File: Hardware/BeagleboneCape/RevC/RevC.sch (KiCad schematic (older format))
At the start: 6 parts, among them P1 CONN_02X04, P2 CONN_01X12, P8 BeagleBone_Black_Header, P9 BeagleBone_Black_Header

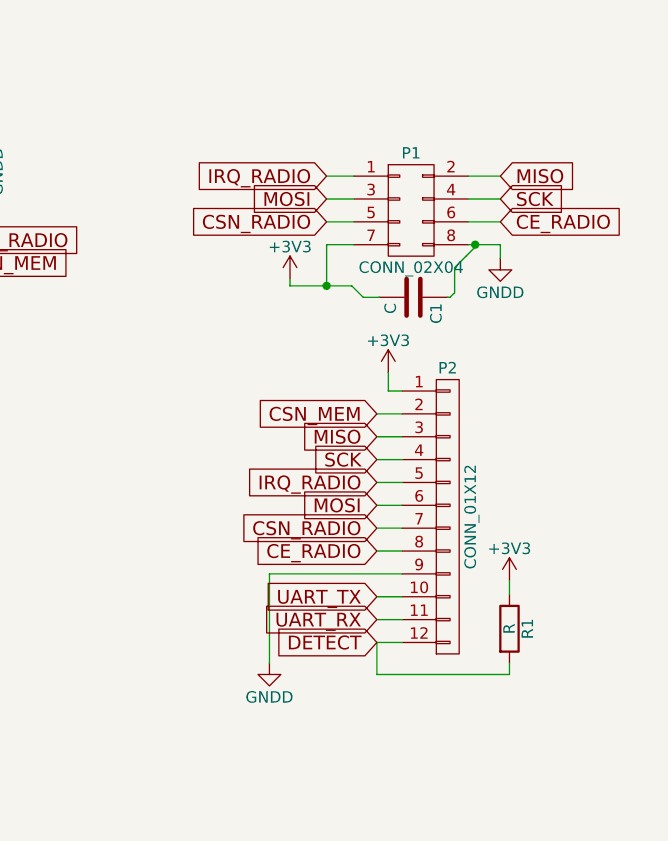
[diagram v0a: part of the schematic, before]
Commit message: initial mockup of board layout, removed 8 pin connector in favour of the single-module board
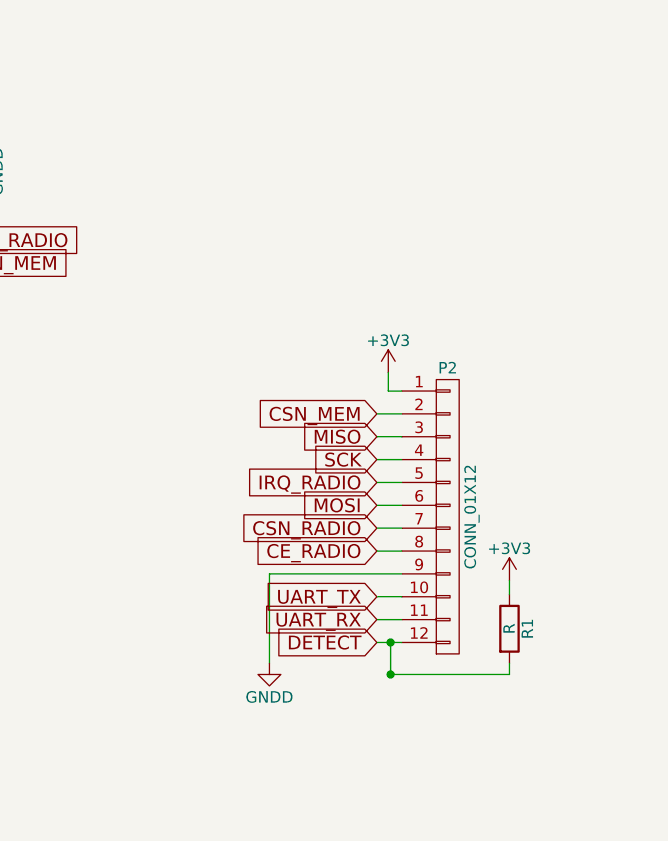
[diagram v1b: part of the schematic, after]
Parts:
- removed C1: C, Capacitors_SMD:C_1210_HandSoldering, symbol C
- removed P1: CONN_02X04, Pin_Headers:Pin_Header_Straight_2x04, symbol CONN_02X04
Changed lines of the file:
@@
 CE_RADIO
-$Comp
-L CONN_02X04 P1
-U 1 1 56935EF2
-P 7610 1320
-F 0 "P1" H 7610 1570 50  0000 C CNN
-F 1 "CONN_02X04" H 7610 1070 50  0000 C CNN
-F 2 "Pin_Headers:Pin_Header_Straight_2x04" H 7610 120 50  0001 C CNN
-F 3 "" H 7610 120 50  0000 C CNN
-	1    7610 1320
-	1    0    0    -1
-$EndComp
-Wire Wire Line
-	7360 1170 7240 1170
-Wire Wire Line
-	7360 1270 7240 1270
-Wire Wire Line
-	7360 1370 7240 1370
-Wire Wire Line
-	7240 1470 7360 1470
-Wire Wire Line
-	7860 1170 8000 1170
-Wire Wire Line
-	7860 1270 8000 1270
-Wire Wire Line
-	7860 1370 8000 1370
-Wire Wire Line
-	7860 1470 8000 1470
-Text GLabel 7240 1170 0    60   Input ~ 0
-IRQ_RADIO
-Text GLabel 7240 1270 0    60   Input ~ 0
-MOSI
-Text GLabel 7240 1370 0    60   Input ~ 0
-CSN_RADIO
-Text GLabel 8000 1170 2    60   Input ~ 0
-MISO
-Text GLabel 8000 1270 2    60   Input ~ 0
-SCK
-Text GLabel 8000 1370 2    60   Input ~ 0
-CE_RADIO
-$Comp
-L GNDD #PWR014
-U 1 1 569364C3
-P 8000 1530
-F 0 "#PWR014" H 8000 1280 50  0001 C CNN
-F 1 "GNDD" H 8000 1380 50  0000 C CNN
-F 2 "" H 8000 1530 60  0000 C CNN
-F 3 "" H 8000 1530 60  0000 C CNN
-	1    8000 1530
-	1    0    0    -1
-$EndComp
-Wire Wire Line
-	8000 1470 8000 1530
-$Comp
-L +3V3 #PWR015
-U 1 1 56936787
-P 7080 1620
-F 0 "#PWR015" H 7080 1470 50  0001 C CNN
-F 1 "+3V3" H 7080 1760 50  0000 C CNN
-F 2 "" H 7080 1620 60  0000 C CNN
-F 3 "" H 7080 1620 60  0000 C CNN
-	1    7080 1620
-	1    0    0    -1
-$EndComp
-Wire Wire Line
-	7080 1620 7080 1650
-Wire Wire Line
-	7080 1650 7350 1650
-Wire Wire Line
-	7240 1650 7240 1470
-$Comp
-L C C1
-U 1 1 569368DA
-P 7620 1700
-F 0 "C1" H 7645 1800 50  0000 L CNN
-F 1 "C" H 7645 1600 50  0000 L CNN
-F 2 "Capacitors_SMD:C_1210_HandSoldering" H 7658 1550 50  0001 C CNN
-F 3 "" H 7620 1700 50  0000 C CNN
-	1    7620 1700
-	0    1    1    0
-$EndComp
-Wire Wire Line
-	7850 1520 7890 1480
-Wire Wire Line
-	7890 1480 7890 1470
-Connection ~ 7890 1470
-Wire Wire Line
-	7350 1650 7400 1700
-Wire Wire Line
-	7400 1700 7470 1700
-Connection ~ 7240 1650
-Wire Wire Line
-	7850 1520 7800 1570
-Wire Wire Line
-	7800 1570 7800 1680
-Wire Wire Line
-	7800 1680 7780 1700
-Wire Wire Line
-	7780 1700 7770 1700
 $Comp
 L CONN_01X12 P2
@@
 Wire Wire Line
 	7510 2030 7510 2110
-Wire Wire Line
-	7510 2110 7570 2110
 Wire Wire Line
 	7570 3210 7460 3210
@@
 $EndComp
 Wire Wire Line
-	7460 3210 7460 3350
-Wire Wire Line
-	7460 3350 8040 3350
-Wire Wire Line
 	8040 3350 8040 3300
 Text GLabel 7460 3210 0    60   Input ~ 0
@@
 Wire Wire Line
 	8040 2940 8040 3000
+Wire Wire Line
+	7520 3350 7520 3210
+Connection ~ 7520 3210
+Connection ~ 7520 3350
+Wire Wire Line
+	7520 3350 8040 3350
+Wire Wire Line
+	7510 2110 7570 2110
 $EndSCHEMATC

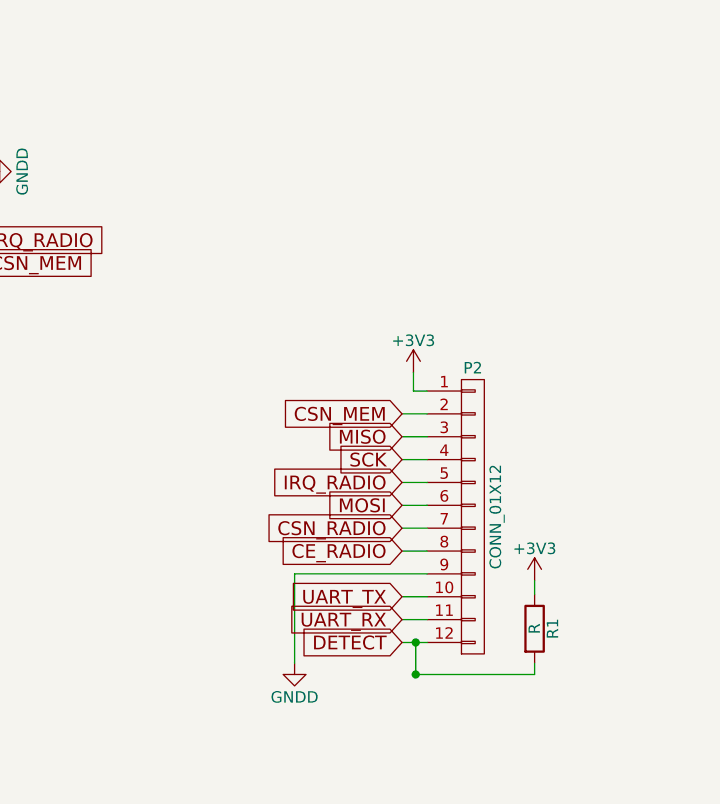
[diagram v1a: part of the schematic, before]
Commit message: updated layout to include radio header thanks to new layout tweaks
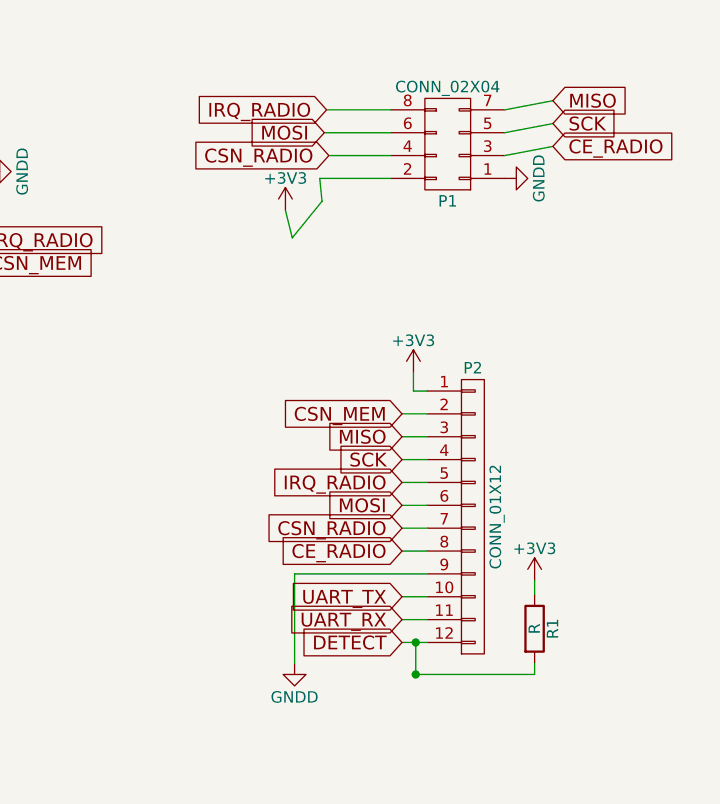
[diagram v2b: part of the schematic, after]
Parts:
- added P1: CONN_02X04, Pin_Headers:Pin_Header_Straight_2x04, symbol CONN_02X04
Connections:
- net +3V3: now also P1.2 (P2)
- net CE_RADIO: now also P1.3 (P3)
- net CSN_RADIO: now also P1.4 (P4)
- net GNDD: now also P1.1 (P1)
- net IRQ_RADIO: now also P1.8 (P8)
- net MISO: now also P1.7 (P7)
- net MOSI: now also P1.6 (P6)
- net SCK: now also P1.5 (P5)
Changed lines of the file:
@@
 $EndComp
 $Comp
-L +3V3 #PWR016
+L +3V3 #PWR014
 U 1 1 569370A7
 P 7510 2030
-F 0 "#PWR016" H 7510 1880 50  0001 C CNN
+F 0 "#PWR014" H 7510 1880 50  0001 C CNN
 F 1 "+3V3" H 7510 2170 50  0000 C CNN
 F 2 "" H 7510 2030 60  0000 C CNN
@@
 $EndComp
 $Comp
-L GNDD #PWR017
+L GNDD #PWR015
 U 1 1 569370C1
 P 6990 3300
-F 0 "#PWR017" H 6990 3050 50  0001 C CNN
+F 0 "#PWR015" H 6990 3050 50  0001 C CNN
 F 1 "GNDD" H 6990 3150 50  0000 C CNN
 F 2 "" H 6990 3300 60  0000 C CNN
@@
 	7510 2030 7510 2110
 Wire Wire Line
-	7570 3210 7460 3210
+	7460 3210 7570 3210
 Wire Wire Line
 	7570 2210 7460 2210
@@
 NoConn ~ 1380 4510
 $Comp
-L PWR_FLAG #FLG018
+L PWR_FLAG #FLG016
 U 1 1 56939577
 P 2850 720
-F 0 "#FLG018" H 2850 815 50  0001 C CNN
+F 0 "#FLG016" H 2850 815 50  0001 C CNN
 F 1 "PWR_FLAG" H 2850 900 50  0000 C CNN
 F 2 "" H 2850 720 50  0000 C CNN
@@
 $EndComp
 $Comp
-L PWR_FLAG #FLG019
+L PWR_FLAG #FLG017
 U 1 1 56939598
 P 3050 710
-F 0 "#FLG019" H 3050 805 50  0001 C CNN
+F 0 "#FLG017" H 3050 805 50  0001 C CNN
 F 1 "PWR_FLAG" H 3050 890 50  0000 C CNN
 F 2 "" H 3050 710 50  0000 C CNN
@@
 $EndComp
 $Comp
-L PWR_FLAG #FLG020
+L PWR_FLAG #FLG018
 U 1 1 569395B2
 P 3290 720
-F 0 "#FLG020" H 3290 815 50  0001 C CNN
+F 0 "#FLG018" H 3290 815 50  0001 C CNN
 F 1 "PWR_FLAG" H 3290 900 50  0000 C CNN
 F 2 "" H 3290 720 50  0000 C CNN
@@
 $EndComp
 $Comp
-L PWR_FLAG #FLG021
+L PWR_FLAG #FLG019
 U 1 1 569395CC
 P 3790 1060
-F 0 "#FLG021" H 3790 1155 50  0001 C CNN
+F 0 "#FLG019" H 3790 1155 50  0001 C CNN
 F 1 "PWR_FLAG" H 3790 1240 50  0000 C CNN
 F 2 "" H 3790 1060 50  0000 C CNN
@@
 $EndComp
 $Comp
-L PWR_FLAG #FLG022
+L PWR_FLAG #FLG020
 U 1 1 56939898
 P 3500 2510
-F 0 "#FLG022" H 3500 2605 50  0001 C CNN
+F 0 "#FLG020" H 3500 2605 50  0001 C CNN
 F 1 "PWR_FLAG" H 3500 2690 50  0000 C CNN
 F 2 "" H 3500 2510 50  0000 C CNN
@@
 $EndComp
 $Comp
-L PWR_FLAG #FLG023
+L PWR_FLAG #FLG021
 U 1 1 569398B2
 P 3710 2800
-F 0 "#FLG023" H 3710 2895 50  0001 C CNN
+F 0 "#FLG021" H 3710 2895 50  0001 C CNN
 F 1 "PWR_FLAG" H 3710 2980 50  0000 C CNN
 F 2 "" H 3710 2800 50  0000 C CNN
@@
 NoConn ~ 5400 2050
 $Comp
-L +3V3 #PWR024
+L +3V3 #PWR022
 U 1 1 5693E0F6
 P 8040 2940
-F 0 "#PWR024" H 8040 2790 50  0001 C CNN
+F 0 "#PWR022" H 8040 2790 50  0001 C CNN
 F 1 "+3V3" H 8040 3080 50  0000 C CNN
 F 2 "" H 8040 2940 60  0000 C CNN
@@
 Wire Wire Line
 	7510 2110 7570 2110
+$Comp
+L CONN_02X04 P1
+U 1 1 56955225
+P 7660 1030
+F 0 "P1" H 7660 1280 50  0000 C CNN
+F 1 "CONN_02X04" H 7660 780 50  0000 C CNN
+F 2 "Pin_Headers:Pin_Header_Straight_2x04" H 7660 -170 50  0001 C CNN
+F 3 "" H 7660 -170 50  0000 C CNN
+	1    7660 1030
+	-1   0    0    1
+$EndComp
+Wire Wire Line
+	7410 880  7130 880
+Wire Wire Line
+	7410 980  7120 980
+Wire Wire Line
+	7410 1080 7140 1080
+Wire Wire Line
+	7410 1180 7100 1180
+Text GLabel 7130 880  0    60   Input ~ 0
+IRQ_RADIO
+Text GLabel 7120 980  0    60   Input ~ 0
+MOSI
+Text GLabel 7140 1080 0    60   Input ~ 0
+CSN_RADIO
+$Comp
+L +3V3 #PWR023
+U 1 1 56955580
+P 6950 1320
+F 0 "#PWR023" H 6950 1170 50  0001 C CNN
+F 1 "+3V3" H 6950 1460 50  0000 C CNN
+F 2 "" H 6950 1320 60  0000 C CNN
+F 3 "" H 6950 1320 60  0000 C CNN
+	1    6950 1320
+	1    0    0    -1
+$EndComp
+Wire Wire Line
+	7100 1180 7110 1280
+Wire Wire Line
+	7110 1280 6980 1440
+Wire Wire Line
+	6980 1440 6950 1320
+$Comp
+L GNDD #PWR024
+U 1 1 5695561F
+P 7910 1180
+F 0 "#PWR024" H 7910 930 50  0001 C CNN
+F 1 "GNDD" H 7910 1030 50  0000 C CNN
+F 2 "" H 7910 1180 60  0000 C CNN
+F 3 "" H 7910 1180 60  0000 C CNN
+	1    7910 1180
+	0    -1   -1   0
+$EndComp
+Wire Wire Line
+	7910 1080 8120 1040
+Wire Wire Line
+	7910 980  8120 940
+Wire Wire Line
+	7910 880  8120 840
+Text GLabel 8120 840  2    60   Input ~ 0
+MISO
+Text GLabel 8120 940  2    60   Input ~ 0
+SCK
+Text GLabel 8120 1040 2    60   Input ~ 0
+CE_RADIO
 $EndSCHEMATC
